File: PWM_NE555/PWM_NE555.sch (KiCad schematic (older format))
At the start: 1 part

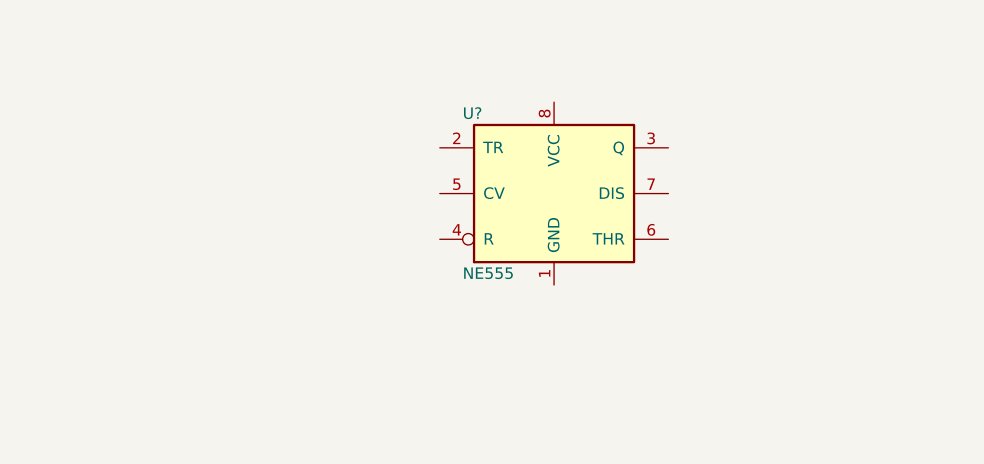
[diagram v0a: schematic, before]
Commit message: Made NE555 PWM schematic
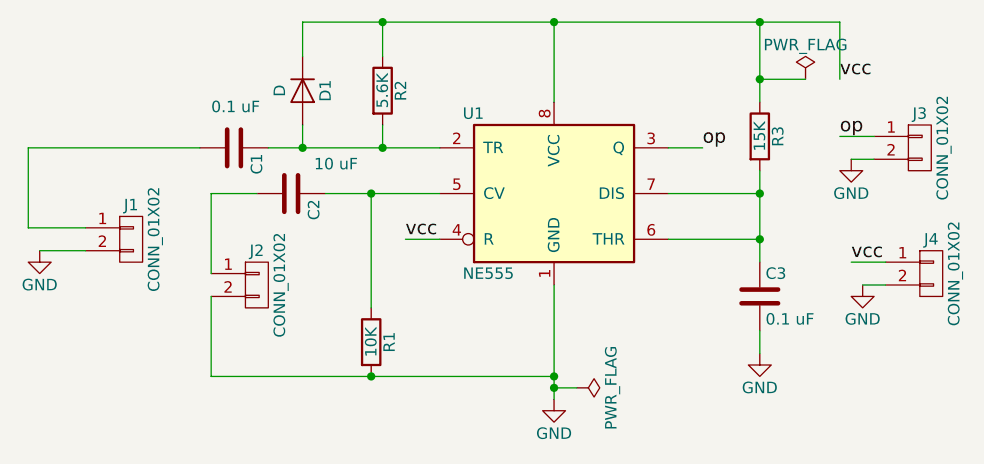
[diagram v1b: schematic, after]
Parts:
- added C1, C3: 0.1 uF, symbol C
- added C2: 10 uF, symbol C
- added D1: D, symbol D
- added J1, J2, J3, J4: CONN_01X02, symbol CONN_01X02
- added R1: 10K, symbol R
- added R2: 5.6K, symbol R
- added R3: 15K, symbol R
- gave numbers to parts that had none: 1
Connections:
- net GND: now reaches U1.1 (GND)
- net GND: now also C3.2, J1.2 (P2), J2.2 (P2), J3.2 (P2), J4.2 (P2), R1.2
- net at U1.2 (TR): now also C1.1, D1.2 (A), R2.2
- net op: now reaches U1.3 (Q)
- net op: now also J3.1 (P1)
- net vcc: now reaches U1.4 (R)
- net vcc: now also U1.8 (VCC), D1.1 (K), J4.1 (P1), R2.1, R3.1
- net at U1.5 (CV): now also C2.1, R1.1
- net at U1.6 (THR): now also U1.7 (DIS), C3.1, R3.2
- new net: C1.2, J1.1 (P1)
- new net: C2.2, J2.1 (P1)

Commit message: Added Footprints to the Schematic Components
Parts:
- C1, C2, C3: footprint (none) -> Capacitors_THT:C_Disc_D3.0mm_W2.0mm_P2.50mm
- D1: footprint (none) -> Diodes_THT:D_DO-201AD_P15.24mm_Horizontal
- J1, J2, J3, J4: footprint (none) -> Connectors_Terminal_Blocks:TerminalBlock_Pheonix_MKDS1.5-2pol
- R1, R2, R3: footprint (none) -> Resistors_THT:R_Axial_DIN0207_L6.3mm_D2.5mm_P15.24mm_Horizontal
- U1: footprint (none) -> Housings_DIP:DIP-8_W7.62mm
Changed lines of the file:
@@
 F 0 "U1" H 4250 1900 50  0000 L CNN
 F 1 "NE555" H 4250 1200 50  0000 L CNN
-F 2 "" H 4650 1550 50  0001 C CNN
+F 2 "Housings_DIP:DIP-8_W7.62mm" H 4650 1550 50  0001 C CNN
 F 3 "" H 4650 1550 50  0001 C CNN
 	1    4650 1550
@@
 F 0 "J1" H 2800 1900 50  0000 C CNN
 F 1 "CONN_01X02" V 2900 1750 50  0000 C CNN
-F 2 "" H 2800 1750 50  0001 C CNN
+F 2 "Connectors_Terminal_Blocks:TerminalBlock_Pheonix_MKDS1.5-2pol" H 2800 1750 50  0001 C CNN
 F 3 "" H 2800 1750 50  0001 C CNN
 	1    2800 1750
@@
 F 0 "J2" H 3350 2100 50  0000 C CNN
 F 1 "CONN_01X02" V 3450 1950 50  0000 C CNN
-F 2 "" H 3350 1950 50  0001 C CNN
+F 2 "Connectors_Terminal_Blocks:TerminalBlock_Pheonix_MKDS1.5-2pol" H 3350 1950 50  0001 C CNN
 F 3 "" H 3350 1950 50  0001 C CNN
 	1    3350 1950
@@
 F 0 "J4" H 6300 2050 50  0000 C CNN
 F 1 "CONN_01X02" V 6400 1900 50  0000 C CNN
-F 2 "" H 6300 1900 50  0001 C CNN
+F 2 "Connectors_Terminal_Blocks:TerminalBlock_Pheonix_MKDS1.5-2pol" H 6300 1900 50  0001 C CNN
 F 3 "" H 6300 1900 50  0001 C CNN
 	1    6300 1900
@@
 F 0 "J3" H 6250 1500 50  0000 C CNN
 F 1 "CONN_01X02" V 6350 1350 50  0000 C CNN
-F 2 "" H 6250 1350 50  0001 C CNN
+F 2 "Connectors_Terminal_Blocks:TerminalBlock_Pheonix_MKDS1.5-2pol" H 6250 1350 50  0001 C CNN
 F 3 "" H 6250 1350 50  0001 C CNN
 	1    6250 1350
@@
 F 0 "C1" H 3275 1450 50  0000 L CNN
 F 1 "0.1 uF" V 3100 1250 50  0000 L BNN
-F 2 "" H 3288 1200 50  0001 C CNN
+F 2 "Capacitors_THT:C_Disc_D3.0mm_W2.0mm_P2.50mm" H 3288 1200 50  0001 C CNN
 F 3 "" H 3250 1350 50  0001 C CNN
 	1    3250 1350
@@
 F 0 "C3" H 5575 2100 50  0000 L CNN
 F 1 "0.1 uF" H 5575 1900 50  0000 L CNN
-F 2 "" H 5588 1850 50  0001 C CNN
+F 2 "Capacitors_THT:C_Disc_D3.0mm_W2.0mm_P2.50mm" H 5588 1850 50  0001 C CNN
 F 3 "" H 5550 2000 50  0001 C CNN
 	1    5550 2000
@@
 F 0 "C2" H 3525 1650 50  0000 L CNN
 F 1 "10 uF" V 3400 1650 50  0000 L BNN
-F 2 "" H 3538 1400 50  0001 C CNN
+F 2 "Capacitors_THT:C_Disc_D3.0mm_W2.0mm_P2.50mm" H 3538 1400 50  0001 C CNN
 F 3 "" H 3500 1550 50  0001 C CNN
 	1    3500 1550
@@
 F 0 "R2" V 3980 1100 50  0000 C CNN
 F 1 "5.6K" V 3900 1100 50  0000 C CNN
-F 2 "" V 3830 1100 50  0001 C CNN
+F 2 "Resistors_THT:R_Axial_DIN0207_L6.3mm_D2.5mm_P15.24mm_Horizontal" V 3830 1100 50  0001 C CNN
 F 3 "" H 3900 1100 50  0001 C CNN
 	1    3900 1100
@@
 F 0 "R3" V 5630 1300 50  0000 C CNN
 F 1 "15K" V 5550 1300 50  0000 C CNN
-F 2 "" V 5480 1300 50  0001 C CNN
+F 2 "Resistors_THT:R_Axial_DIN0207_L6.3mm_D2.5mm_P15.24mm_Horizontal" V 5480 1300 50  0001 C CNN
 F 3 "" H 5550 1300 50  0001 C CNN
 	1    5550 1300
@@
 F 0 "R1" V 3930 2200 50  0000 C CNN
 F 1 "10K" V 3850 2200 50  0000 C CNN
-F 2 "" V 3780 2200 50  0001 C CNN
+F 2 "Resistors_THT:R_Axial_DIN0207_L6.3mm_D2.5mm_P15.24mm_Horizontal" V 3780 2200 50  0001 C CNN
 F 3 "" H 3850 2200 50  0001 C CNN
 	1    3850 2200
@@
 F 0 "D1" H 3550 1200 50  0000 C CNN
 F 1 "D" H 3550 1000 50  0000 C CNN
-F 2 "" H 3550 1100 50  0001 C CNN
+F 2 "Diodes_THT:D_DO-201AD_P15.24mm_Horizontal" H 3550 1100 50  0001 C CNN
 F 3 "" H 3550 1100 50  0001 C CNN
 	1    3550 1100
